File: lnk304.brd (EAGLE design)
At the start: 49.5 x 24.5 mm, 25 parts

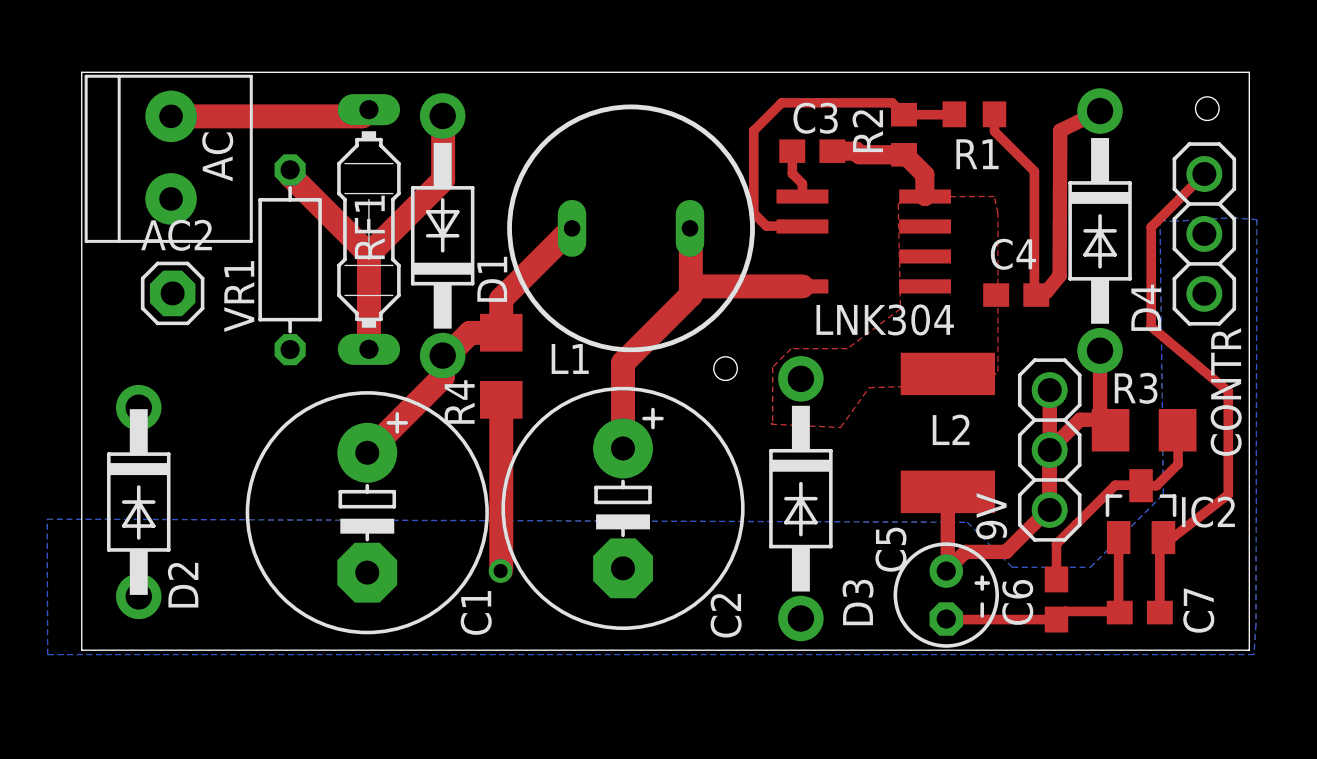
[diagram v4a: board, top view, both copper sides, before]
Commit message: Added passive componets' values which were removed by mistake
** 27.Mar.2016 **

Schematic:
- Added passive componets' values which were removed by mistake

PCB Layout:
- Smash passive components and remove passive components' values

-- Missing --
- Need to add hot and neutral pins for AC plug concept
- Need to revise Terminal Block size and overlapping with D2
- May need to increase L2 pad distance a bit
- May need to decrease the board height by 2mm
- Add Creepage between C1 and C2 pads
- Revise the two holes diameter and availability of screws
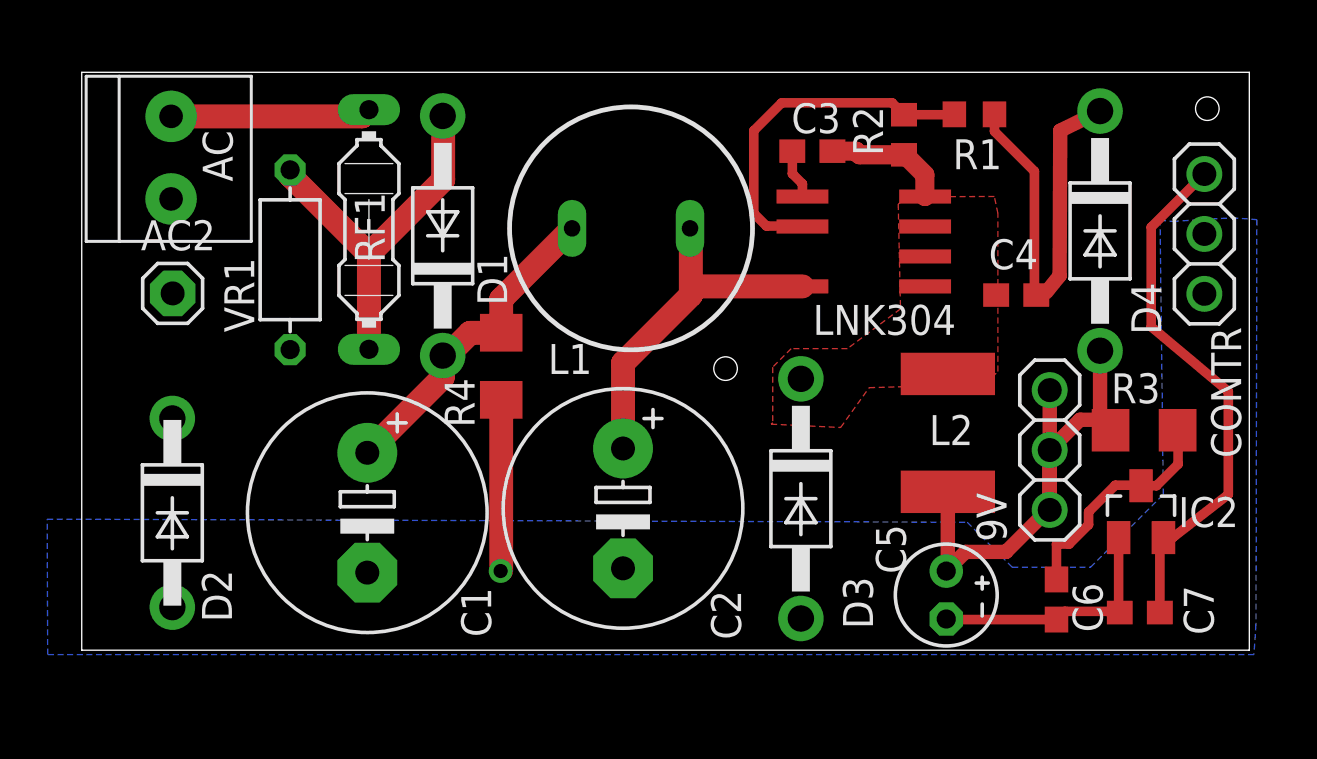
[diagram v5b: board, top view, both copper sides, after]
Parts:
- C3: value (none) -> 0.1 uF
- C4: value (none) -> 10 uF
- C5: value (none) -> 100 uF
- C6, C7: value (none) -> 1 uF
- L1: value (none) -> 1000 uH
- L2: value (none) -> 680 uH
- R1: value (none) -> 9.1k
- R2: value (none) -> 2k
- R3: value (none) -> 10
- moved D2 1.49 mm to (3.84, 5.82)
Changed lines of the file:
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@@
 <element name="C2" library="adafruit" package="E5-10,5" value="4.7 uF" x="22.948" y="6.011" smashed="yes" rot="R270">
 <attribute name="NAME" x="26.6832" y="2.5404" size="1.27" layer="25" ratio="10" rot="R270"/>
-<attribute name="VALUE" x="19.7222" y="9.1352" size="1.27" layer="27" ratio="10" rot="R270"/>
+<attribute name="VALUE" x="19.9594375" y="8.62034375" size="1.27" layer="27" ratio="10" rot="R270"/>
 </element>
 <element name="D1" library="adafruit" package="DO41-10" value="1N4007" x="15.303" y="17.57" smashed="yes" rot="R90">
@@
 <attribute name="VALUE" x="18.097" y="17.625" size="1.27" layer="27" ratio="10" rot="R90"/>
 </element>
-<element name="D2" library="adafruit" package="DO41-7" value="1N4007" x="2.418" y="6.281" smashed="yes" rot="R270">
-<attribute name="NAME" x="3.675" y="3.859" size="1.27" layer="25" ratio="10" rot="R270"/>
-<attribute name="VALUE" x="4.015" y="13.162" size="1.27" layer="27" ratio="10" rot="R270"/>
-</element>
-<element name="L1" library="inductor-neosid" package="BS11" value="" x="23.288" y="17.883" smashed="yes">
+<element name="D2" library="adafruit" package="DO41-7" value="1N4007" x="3.841415625" y="5.824815625" smashed="yes" rot="R270">
+<attribute name="NAME" x="5.098415625" y="3.402815625" size="1.27" layer="25" ratio="10" rot="R270"/>
+<attribute name="VALUE" x="5.438415625" y="12.705815625" size="1.27" layer="27" ratio="10" rot="R270"/>
+</element>
+<element name="L1" library="inductor-neosid" package="BS11" value="1000 uH" x="23.288" y="17.883" smashed="yes">
 <attribute name="OC_NEWARK" value="unknown" x="23.288" y="17.883" size="1.778" layer="27" display="off"/>
 <attribute name="OC_FARNELL" value="unknown" x="23.288" y="17.883" size="1.778" layer="27" display="off"/>
@@
 <attribute name="OC_NEWARK" value="unknown" x="12.176" y="17.835" size="1.778" layer="27" rot="R270" display="off"/>
 <attribute name="NAME" x="11.578" y="19.416" size="1.27" layer="25" ratio="10" rot="R270"/>
-<attribute name="VALUE" x="9.6692" y="22.913" size="1.27" layer="27" ratio="10" rot="R270"/>
-</element>
-<element name="C4" library="adafruit" package="C0603" value="" x="39.617" y="15.056" smashed="yes" rot="R180">
+<attribute name="VALUE" x="9.431709375" y="23.38823125" size="1.27" layer="27" ratio="10" rot="R270"/>
+</element>
+<element name="C4" library="adafruit" package="C0603" value="10 uF" x="39.617" y="15.056" smashed="yes" rot="R180">
 <attribute name="NAME" x="40.546" y="17.42" size="1.27" layer="25" rot="R180"/>
-<attribute name="VALUE" x="40.506" y="17.088" size="1.27" layer="27" rot="R180"/>
-</element>
-<element name="C3" library="adafruit" package="C0603" value="" x="30.974" y="21.157"/>
+</element>
+<element name="C3" library="adafruit" package="C0603" value="0.1 uF" x="30.974" y="21.157" smashed="yes">
+<attribute name="NAME" x="30.085" y="21.919" size="1.27" layer="25"/>
+</element>
 <element name="D3" library="adafruit" package="DO41-10" value="SBYV26C" x="30.489" y="6.424" smashed="yes" rot="R270">
 <attribute name="NAME" x="32.275" y="3.11" size="1.27" layer="25" ratio="10" rot="R270"/>
@@
 <attribute name="VALUE" x="44.635" y="23.381" size="1.27" layer="27" ratio="10" rot="R270"/>
 </element>
-<element name="C5" library="adafruit" package="E2-4" value="" x="36.652" y="2.338" smashed="yes" rot="R270">
+<element name="C5" library="adafruit" package="E2-4" value="100 uF" x="36.652" y="2.338" smashed="yes" rot="R270">
 <attribute name="NAME" x="34.941" y="3.239" size="1.27" layer="25" ratio="10" rot="R90"/>
-<attribute name="VALUE" x="34.493" y="0.179" size="1.27" layer="27" ratio="10" rot="R270"/>
-</element>
-<element name="L2" library="rcl" package="L5650M" value="" x="36.719" y="9.213" smashed="yes" rot="R270">
+</element>
+<element name="L2" library="rcl" package="L5650M" value="680 uH" x="36.719" y="9.213" smashed="yes" rot="R270">
 <attribute name="NAME" x="35.925" y="8.696" size="1.27" layer="25"/>
-<attribute name="VALUE" x="32.274" y="11.118" size="1.27" layer="27" rot="R270"/>
-</element>
-<element name="R1" library="adafruit" package="R0603" value="" x="37.846" y="22.717" smashed="yes">
+</element>
+<element name="R1" library="adafruit" package="R0603" value="9.1k" x="37.846" y="22.717" smashed="yes">
 <attribute name="NAME" x="36.928" y="20.391" size="1.27" layer="25"/>
-<attribute name="VALUE" x="36.957" y="20.685" size="1.27" layer="27"/>
-</element>
-<element name="R2" library="adafruit" package="R0603" value="" x="34.86" y="21.851" rot="R90"/>
+</element>
+<element name="R2" library="adafruit" package="R0603" value="2k" x="34.86" y="21.851" smashed="yes" rot="R90">
+<attribute name="NAME" x="33.971" y="20.962" size="1.27" layer="25" rot="R90"/>
+</element>
 <element name="IC2" library="linear" package="SOT23" value="" x="44.909" y="5.873" smashed="yes">
 <attribute name="NAME" x="46.49" y="5.22" size="1.27" layer="25"/>
 <attribute name="VALUE" x="43.004" y="2.698" size="1.27" layer="27"/>
 </element>
-<element name="R3" library="adafruit" package="R1206" value="" x="45.039" y="9.325"/>
-<element name="C6" library="adafruit" package="C0603" value="" x="41.324" y="2.148" smashed="yes" rot="R270">
-<attribute name="NAME" x="39.046" y="3.077" size="1.27" layer="25" rot="R270"/>
-<attribute name="VALUE" x="39.292" y="3.037" size="1.27" layer="27" rot="R270"/>
-</element>
-<element name="C7" library="adafruit" package="C0603" value="" x="44.858" y="1.596" smashed="yes" rot="R180">
+<element name="R3" library="adafruit" package="R1206" value="10" x="45.039" y="9.325" smashed="yes">
+<attribute name="NAME" x="43.642" y="10.468" size="1.27" layer="25"/>
+</element>
+<element name="C6" library="adafruit" package="C0603" value="1 uF" x="41.324" y="2.148" smashed="yes" rot="R270">
+<attribute name="NAME" x="42.011959375" y="2.856021875" size="1.27" layer="25" rot="R270"/>
+</element>
+<element name="C7" library="adafruit" package="C0603" value="1 uF" x="44.858" y="1.596" smashed="yes" rot="R180">
 <attribute name="NAME" x="46.722" y="2.744" size="1.27" layer="25" rot="R270"/>
-<attribute name="VALUE" x="45.747" y="3.628" size="1.27" layer="27" rot="R180"/>
 </element>
 <element name="AC" library="adafruit" package="1X2-3.5MM" value="1X2-3.5MM" x="3.788" y="20.932" smashed="yes" rot="R270">
@@
 <contactref element="VR1" pad="2"/>
 <wire x1="3.854" y1="15.126" x2="8.8346" y2="12.7431" width="0" layer="19" extent="1-1"/>
-<wire x1="2.418" y1="10.281" x2="3.854" y2="15.126" width="0" layer="19" extent="1-1"/>
+<wire x1="3.841415625" y1="9.824815625" x2="3.854" y2="15.126" width="0" layer="19" extent="1-1"/>
 </signal>
 <signal name="N$5">
@@
 <wire x1="46.479" y1="9.307" x2="46.461" y2="9.325" width="0.4064" layer="1"/>
 <wire x1="41.324" y1="2.998" x2="41.324" y2="4.499" width="0.4064" layer="1"/>
-<wire x1="41.324" y1="4.499" x2="43.819" y2="6.994" width="0.4064" layer="1"/>
 <wire x1="43.819" y1="6.994" x2="44.888" y2="6.994" width="0.4064" layer="1"/>
 <wire x1="44.888" y1="6.994" x2="44.909" y2="6.973" width="0.4064" layer="1"/>
+<wire x1="41.324" y1="4.499" x2="41.8631625" y2="4.499" width="0.4064" layer="1"/>
+<wire x1="41.8631625" y1="4.499" x2="42.685715625" y2="5.321553125" width="0.4064" layer="1"/>
+<wire x1="42.685715625" y1="5.321553125" x2="42.685715625" y2="5.860715625" width="0.4064" layer="1"/>
+<wire x1="42.685715625" y1="5.860715625" x2="43.819" y2="6.994" width="0.4064" layer="1"/>
 </signal>
 <signal name="N$14">
@@
 <wire x1="17.7837" y1="3.3819" x2="17.7579" y2="3.3561" width="0.6096" layer="1"/>
 <wire x1="17.7837" y1="3.3819" x2="17.7837" y2="10.6128" width="1.016" layer="1"/>
+<wire x1="30.489" y1="1.344" x2="36.652" y2="1.322" width="0" layer="19" extent="1-1"/>
 </signal>
 <signal name="N$9">

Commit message: Create new PCB layout for AC TBlock and L2
** 8.Apr.2016 **
Created new devices in the library

Schematic:
- Created new library for AC plug
- Added hot and neutral pins for AC plug concept

PCB Layout:
- Revised Terminal Block size and overlapping with D2
- Probably won't need to decrease the board height by 2mm
- Neglect creepage between C1 and C2 pads at the moment
- Increased L2 pad distance a bit by creating a new library ELL-6UH681M
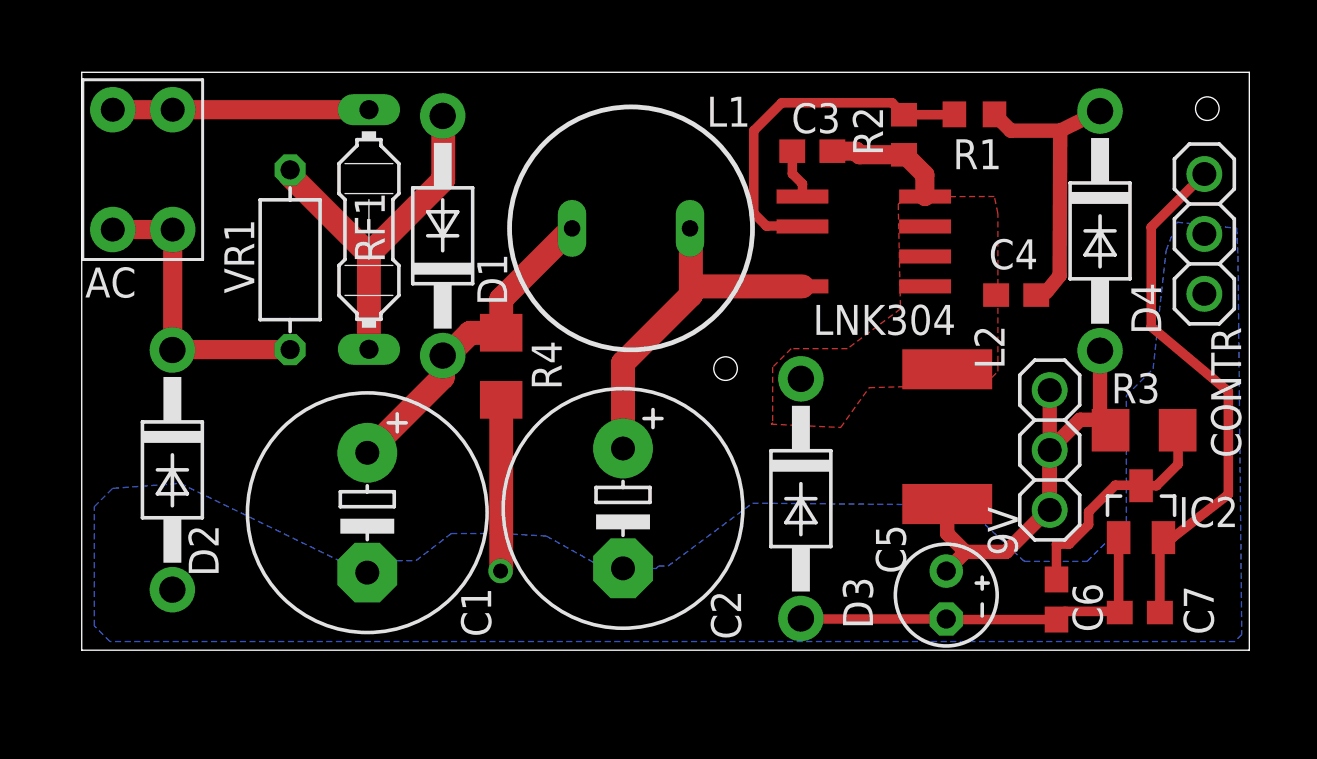
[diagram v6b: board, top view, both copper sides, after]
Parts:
- removed AC2: (no value), adafruit:1X01
- AC: value 1X2-3.5MM -> TBLOCK02X2; device adafruit:1X2-3.5MM -> userdefined:TBLOCK02X2
- D2: device adafruit:DO41-7 -> adafruit:DO41-10
- L2: value 680 uH -> 280 uH; device rcl:L5650M -> userdefined:ELL-6UH681M
- moved D2 1.82 mm to (3.84, 7.65)
- moved AC 1.33 mm to (2.59, 20.4), turned to 0 degrees
- moved L2 0.23 mm to (36.7, 8.99)
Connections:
- removed net N$9: AC.2, RF1.1
- new net N$12: AC.H@1, AC.H@2, RF1.1
- net N$4: now also L2.P$2; no longer L2.2
- net N$6: now also AC.N@1, AC.N@2; no longer AC2.1
- net N$8: now also L2.P$1; no longer L2.1
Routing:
- net N$6: track 0.00 -> 12.7 mm
- net N$12: track 0.00 -> 10.9 mm
- net N$9: track 8.51 -> 0.00 mm
- net GND: track 17.9 -> 24.1 mm
- net N$10: track 17.9 -> 12.6 mm
- net N$4: track 22.9 -> 21.8 mm
